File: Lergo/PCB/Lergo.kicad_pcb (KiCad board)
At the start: 2 copper layers, 96.2 x 95.9 mm, 151 parts, among them J1 MJ-4PP-9, J2 Conn_01x03, J3 Conn_01x08, J4 Conn_01x08, J6 MJ-4PP-9, SW1 SW_PUSH_LED, SW10 SW_PUSH_LED, SW11 SW_PUSH_LED, SW12 SW_PUSH_LED, SW13 SW_PUSH_LED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

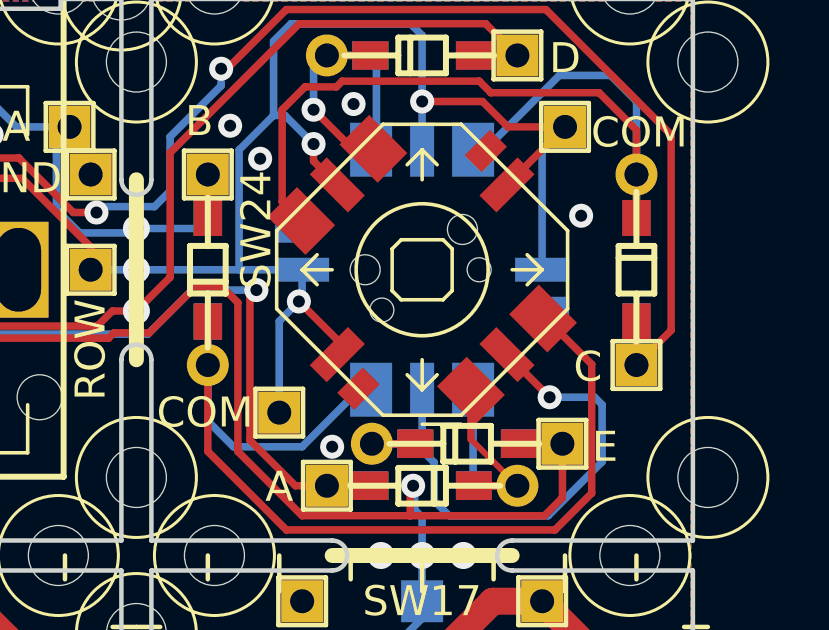
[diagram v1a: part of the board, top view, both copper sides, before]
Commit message: Received 5 way switches. Last minute fixes on silk for clarity
- The no-name 5-way switch is electrically fine. But to avoid confusion with the holes of the top and bottom side (reminder, bottom side is rotated 45 degrees), the corresponding holes on one side have been circled on the side silkscreen.
- The Panasonic 5-way switch is also electrically fine. But this one does not have any keying holes, and it does not have any pin 1 mark... So, for clarity, the "M" and "A23D" markings on the top of the device have been reproduced in the same location on the silkscreen.

Hergo, resinding the previous tag of v1.A and making a new one with this commit. The actual first prototype run will contain these changes.
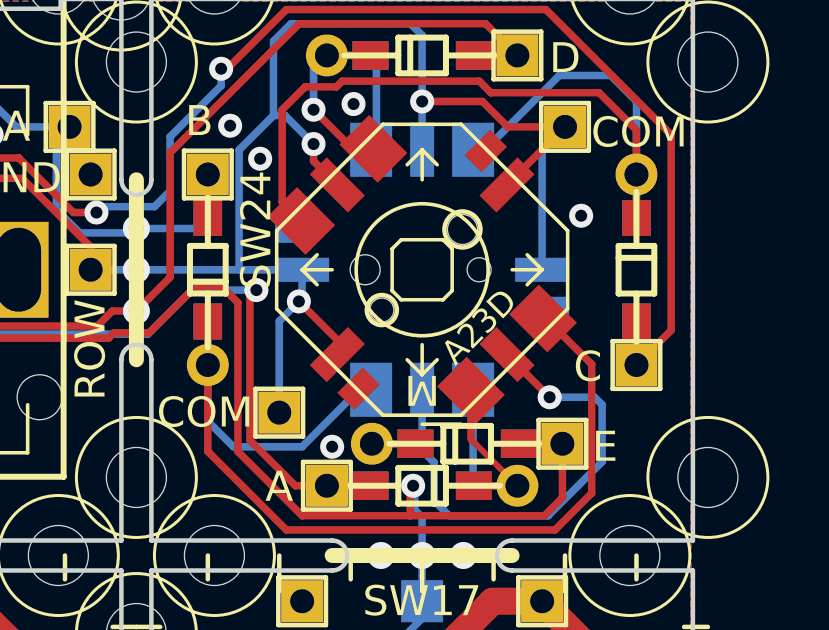
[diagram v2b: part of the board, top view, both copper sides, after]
